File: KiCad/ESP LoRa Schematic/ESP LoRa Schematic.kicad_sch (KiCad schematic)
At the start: 2 parts, among them U1 ESP32-S3-DEVKITC-1-N8R8, U2 RA-02_LORA

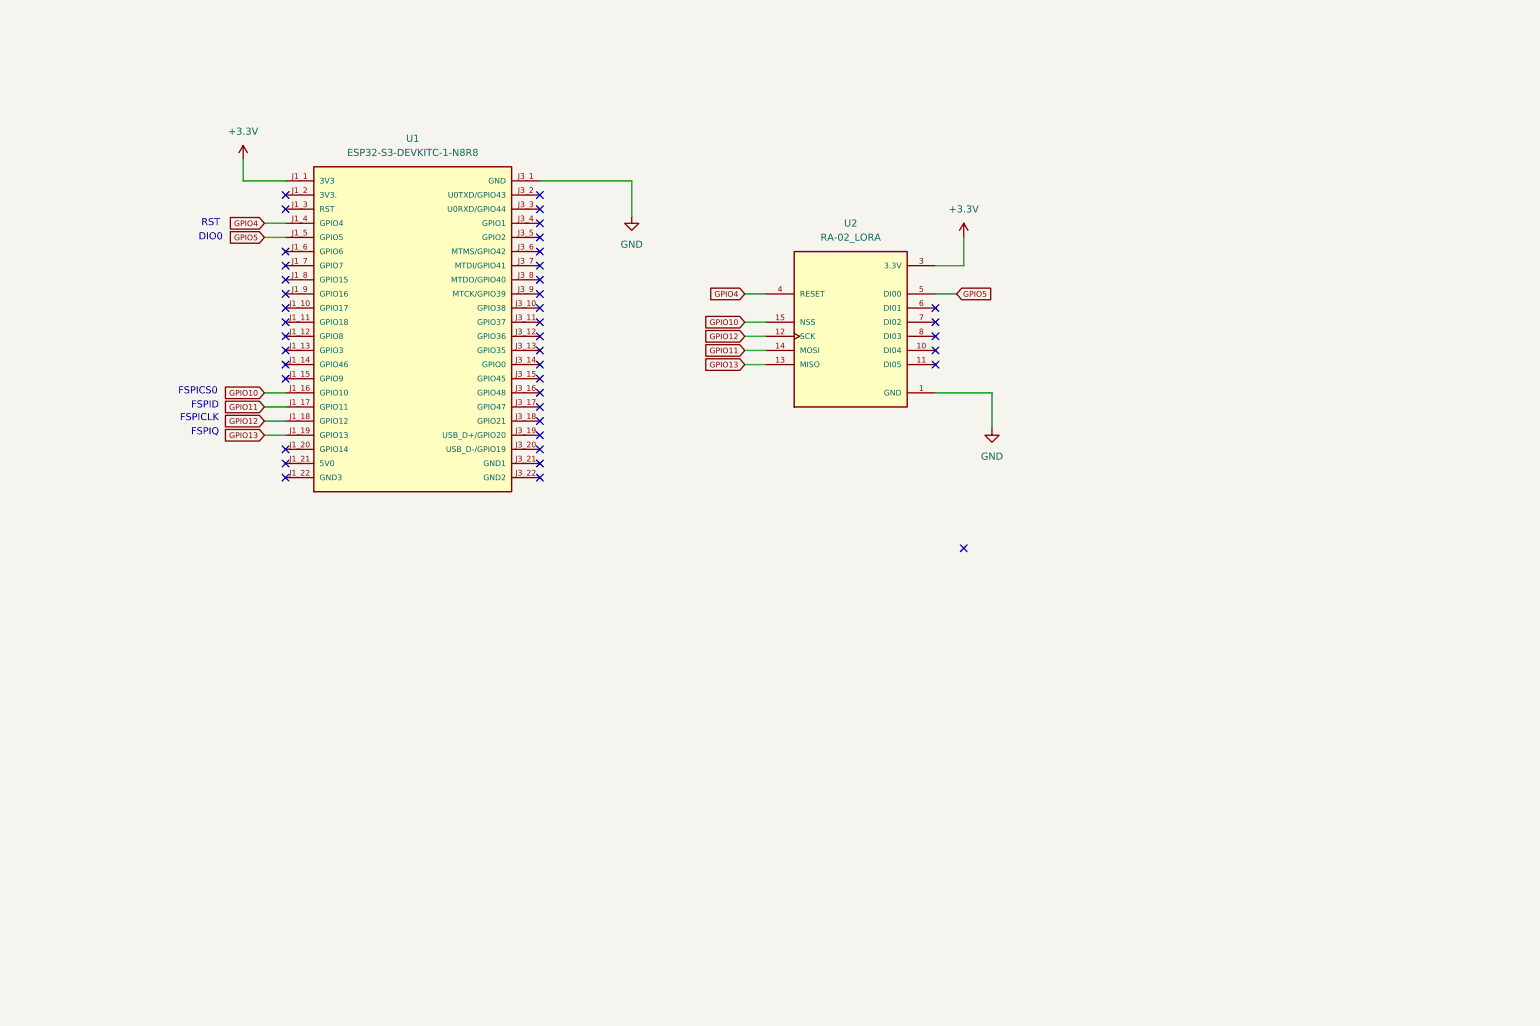
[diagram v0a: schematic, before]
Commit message: Added ECAD feature: Mounting Holes, PCB outline and UWB footprint
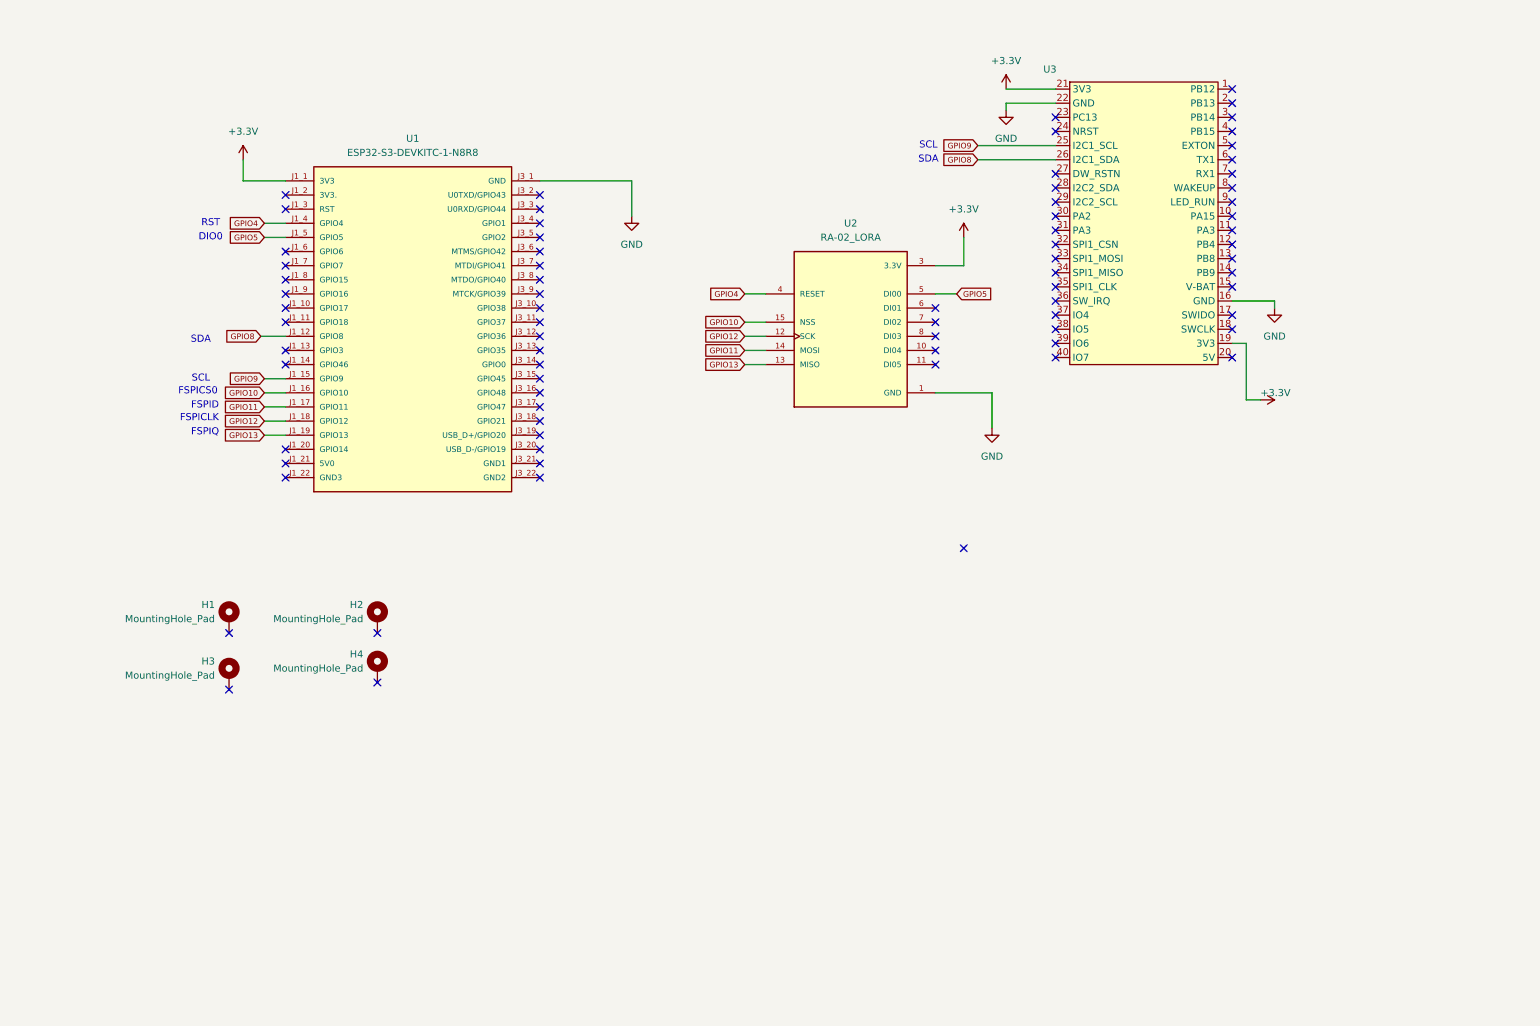
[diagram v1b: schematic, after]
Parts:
- added H1, H2, H3, H4: MountingHole_Pad, MountingHole:MountingHole_4.3mm_M4_DIN965_Pad, symbol Mechanical:MountingHole_Pad
- added U3: ~, Connector_PinSocket_2.54mm:UWB_Female_Headers, symbol Sensor:UWB_DEV
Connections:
- net +3.3V: now also U3.19 (3V3), U3.21 (3V3)
- net GND: now also U3.16 (GND), U3.22 (GND)
- net GPIO8: now reaches U1.J1_12 (GPIO8)
- net GPIO8: now also U3.26 (I2C1_SDA)
- net GPIO9: now reaches U1.J1_15 (GPIO9)
- net GPIO9: now also U3.25 (I2C1_SCL)
- no-connect marks 42 -> 78
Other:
- note added: "SCL"
- note added: "SDA"

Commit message: Add Feature
Two side PCB
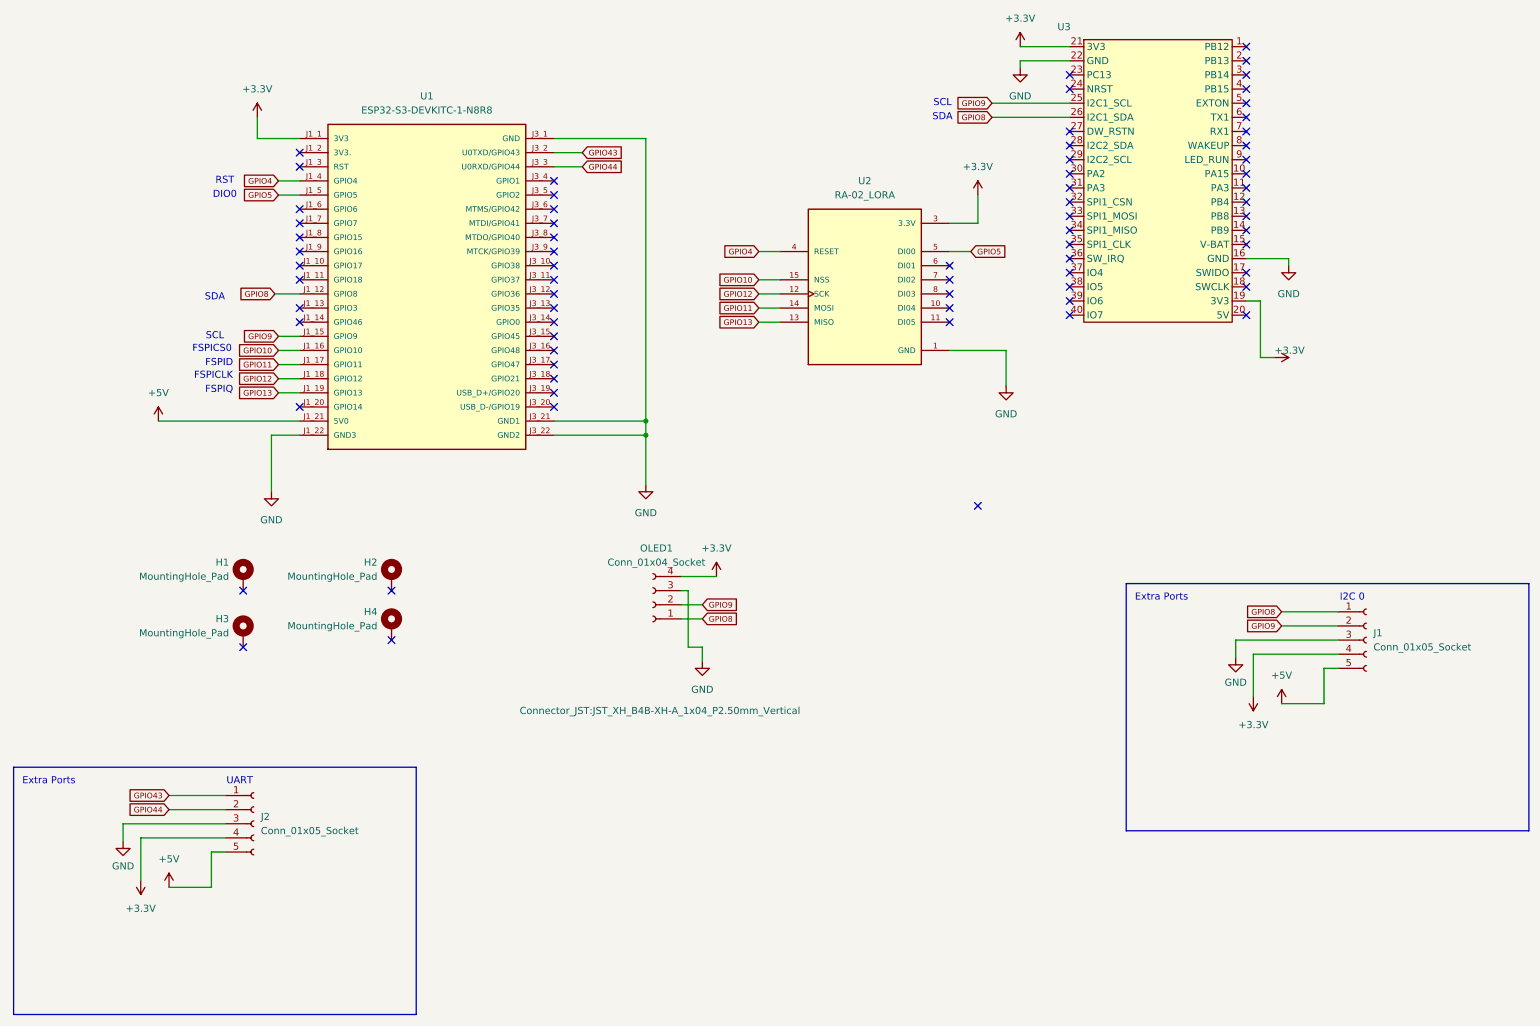
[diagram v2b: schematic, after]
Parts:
- added J1, J2: Conn_01x05_Socket, Connector_JST:JST_XH_B5B-XH-A_1x05_P2.50mm_Vertical, symbol Connector:Conn_01x05_Socket
- added OLED1: Conn_01x04_Socket, Connector_JST:JST_XH_B4B-XH-A_1x04_P2.50mm_Vertical, symbol Connector:Conn_01x04_Socket
- U2: footprint RA-02_LORA:MODULE_RA-02_LORA -> RF:Lora_Dev_Board
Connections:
- net +3.3V: now also J1.4 (Pin_4), J2.4 (Pin_4), OLED1.4 (Pin_4)
- net GND: now also U1.J1_22 (GND3), U1.J3_21 (GND1), U1.J3_22 (GND2), J1.3 (Pin_3), J2.3 (Pin_3), OLED1.3 (Pin_3)
- net GPIO8: now also J1.1 (Pin_1), OLED1.1 (Pin_1)
- net GPIO9: now also J1.2 (Pin_2), OLED1.2 (Pin_2)
- net +5V: now reaches U1.J1_21 (5V0)
- net +5V: now also J1.5 (Pin_5), J2.5 (Pin_5)
- net GPIO43: now reaches U1.J3_2 (U0TXD/GPIO43)
- net GPIO43: now also J2.1 (Pin_1)
- net GPIO44: now reaches U1.J3_3 (U0RXD/GPIO44)
- net GPIO44: now also J2.2 (Pin_2)
- no-connect marks 78 -> 72
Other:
- note added: "Extra Ports"
- note added: "I2C 0"
- note added: "UART"
- moved on the sheet: H1, H2, H3, H4, U1, U2, U3

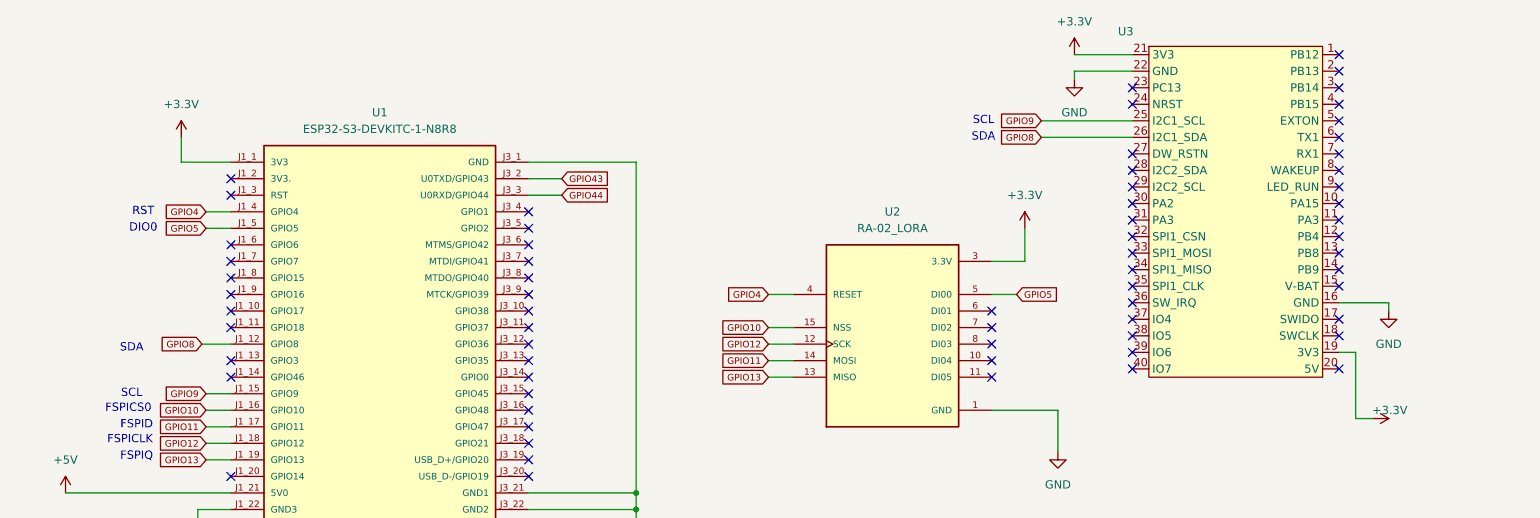
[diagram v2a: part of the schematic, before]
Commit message: chore(schematic): Change UWB pinout
NEEDS UPDATING WITH PA2 AND PA3 PINOUT

change UWB pins to UART on ESP
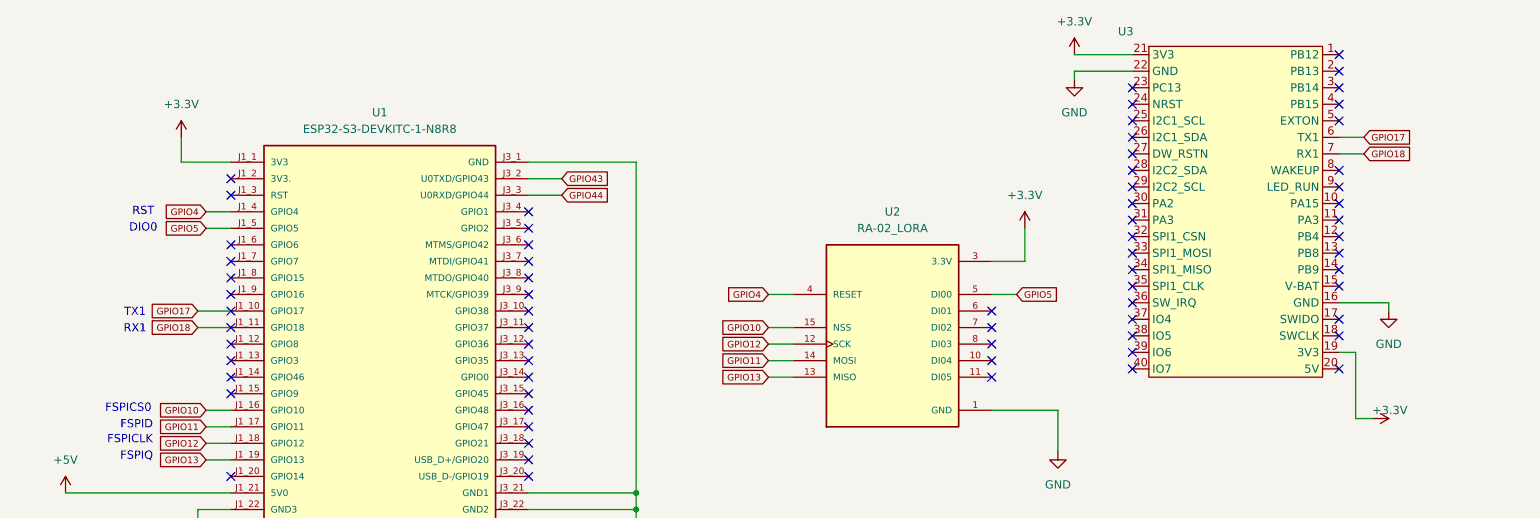
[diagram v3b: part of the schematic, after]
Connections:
- net GPIO8: no longer U1.J1_12 (GPIO8), U3.26 (I2C1_SDA)
- net GPIO9: no longer U1.J1_15 (GPIO9), U3.25 (I2C1_SCL)
- net GPIO17: now reaches U1.J1_10 (GPIO17)
- net GPIO17: now also U3.6 (TX1)
- net GPIO18: now reaches U1.J1_11 (GPIO18)
- net GPIO18: now also U3.7 (RX1)
- no-connect marks 72 -> 74
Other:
- note added: "RX1"
- note added: "TX1"
- note removed: "SCL"
- note removed: "SDA"

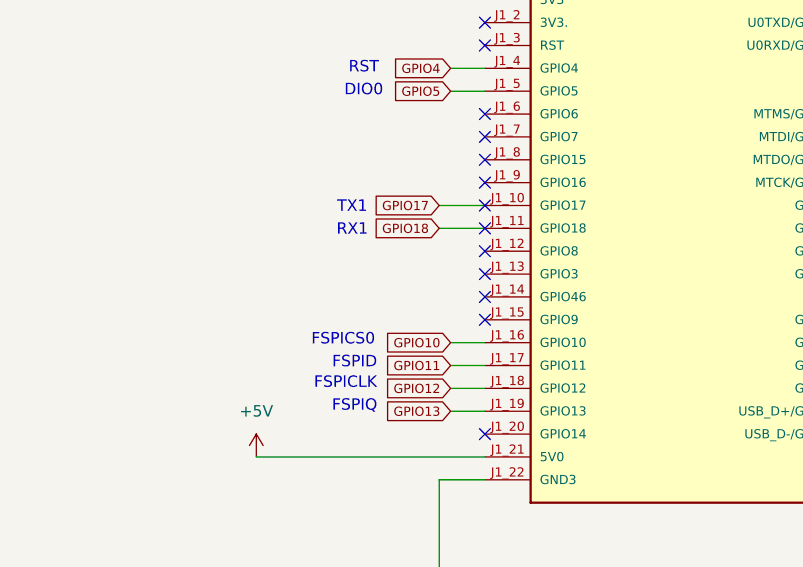
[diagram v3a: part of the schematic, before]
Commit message: Restructure
added a micropythpon pico project
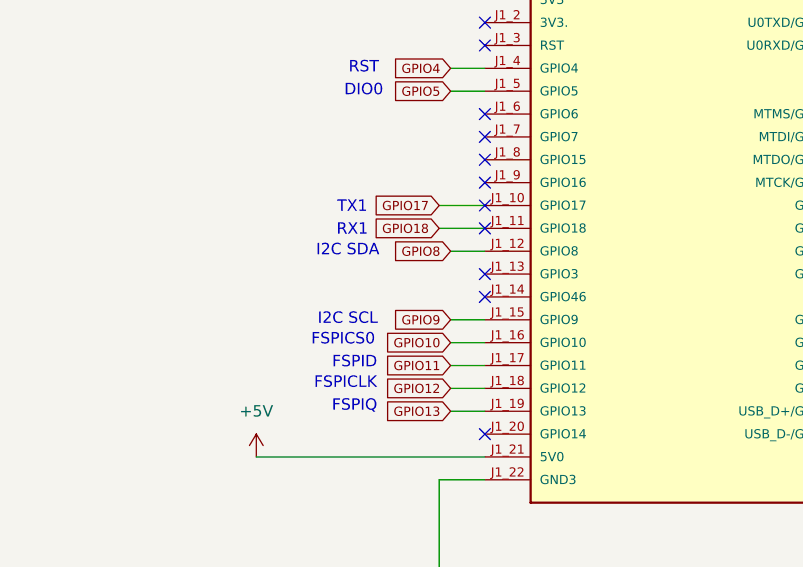
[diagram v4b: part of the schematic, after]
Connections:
- net GPIO8: now also U1.J1_12 (GPIO8)
- net GPIO9: now also U1.J1_15 (GPIO9)
- no-connect marks 74 -> 72
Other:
- note added: "I2C SCL"
- note added: "I2C SDA"
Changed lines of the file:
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@@
+		)
+	)
+	(text "I2C SDA"
+		(exclude_from_sim no)
+		(at 50.8 60.96 0)
+		(effects
+			(font
+				(size 1.27 1.27)
+			)
 		)
 	)
@@
 		(exclude_from_sim no)
 		(at 51.308 56.134 0)
+		(effects
+			(font
+				(size 1.27 1.27)
+			)
+		)
+	)
+	(text "I2C SCL"
+		(exclude_from_sim no)
+		(at 50.8 68.58 0)
 		(effects
 			(font
@@
 	)
 	(no_connect
-		(at 66.04 68.58)
-	)
-	(no_connect
 		(at 236.22 36.83)
 	)
@@
 	)
 	(no_connect
-		(at 66.04 60.96)
-	)
-	(no_connect
 		(at 55.88 114.3)
 	)
@@
 	(wire
 		(pts
+			(xy 62.23 60.96) (xy 66.04 60.96)
+		)
+		(stroke
+			(width 0)
+			(type default)
+		)
+	)
+	(wire
+		(pts
 			(xy 148.59 60.96) (xy 152.4 60.96)
 		)
@@
 	(wire
 		(pts
+			(xy 62.23 68.58) (xy 66.04 68.58)
+		)
+		(stroke
+			(width 0)
+			(type default)
+		)
+	)
+	(wire
+		(pts
 			(xy 187.96 43.18) (xy 187.96 48.26)
 		)
@@
 		)
 	)
+	(global_label "GPIO9"
+		(shape input)
+		(at 62.23 68.58 180)
+		(fields_autoplaced yes)
+		(effects
+			(font
+				(size 1.016 1.016)
+			)
+			(justify right)
+		)
+		(property "Intersheetrefs" "${INTERSHEET_REFS}"
+			(at 55.2943 68.58 0)
+			(effects
+				(font
+					(size 1.27 1.27)
+				)
+				(justify right)
+				(hide yes)
+			)
+		)
+	)
 	(global_label "GPIO5"
 		(shape input)
@@
 			(effects
 				(font
+					(size 1.27 1.27)
+				)
+				(justify right)
+				(hide yes)
+			)
+		)
+	)
+	(global_label "GPIO8"
+		(shape input)
+		(at 62.23 60.96 180)
+		(fields_autoplaced yes)
+		(effects
+			(font
+				(size 1.016 1.016)
+			)
+			(justify right)
+		)
+		(property "Intersheetrefs" "${INTERSHEET_REFS}"
+			(at 55.2943 60.96 0)
+			(effects
+				(font

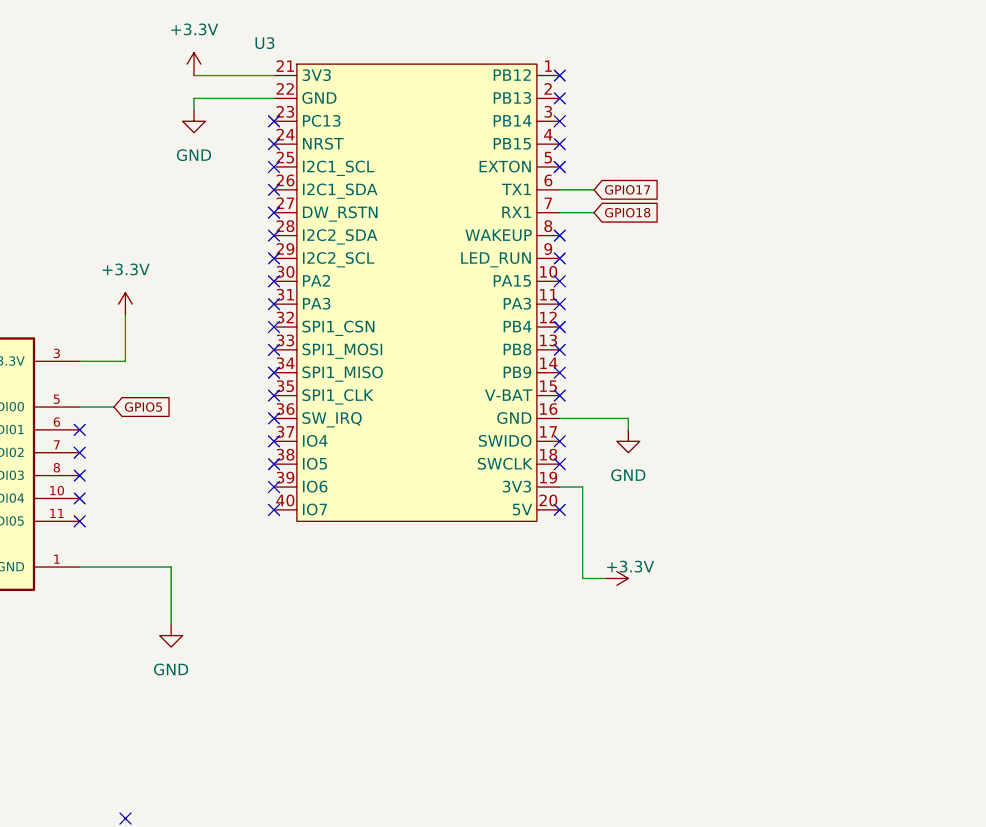
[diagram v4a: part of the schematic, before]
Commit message: add feature
add UWB read data function to main
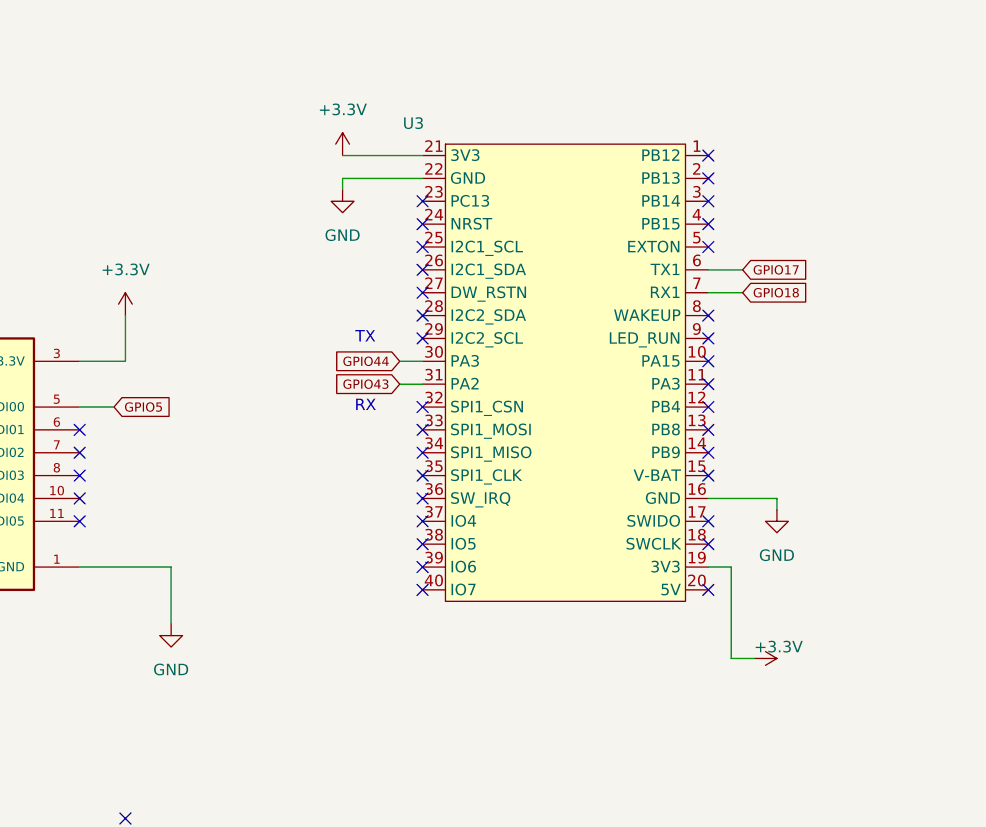
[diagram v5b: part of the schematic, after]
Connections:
- net GPIO43: now also U3.31 (PA2)
- net GPIO44: now also U3.30 (PA3)
- no-connect marks 72 -> 70
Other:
- note added: "RX"
- note added: "TX"
- moved on the sheet: U3
